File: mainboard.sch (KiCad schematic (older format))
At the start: 41 parts

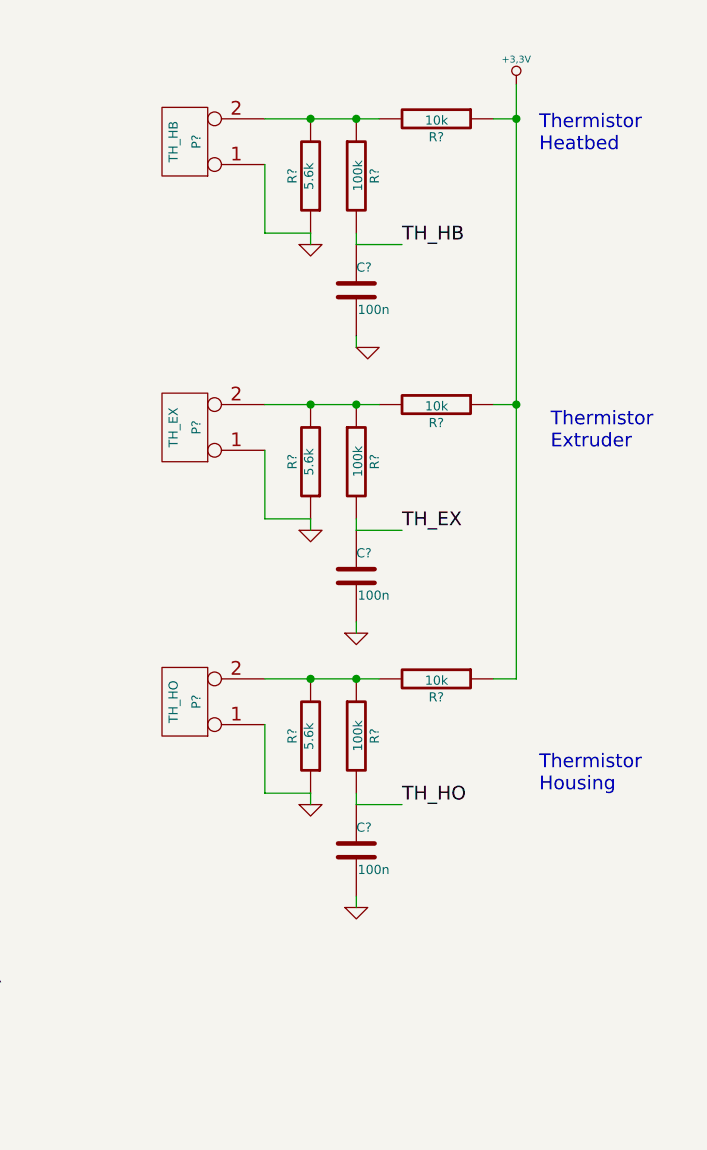
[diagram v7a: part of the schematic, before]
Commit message: Added Pot to trim ADC input for thermistors
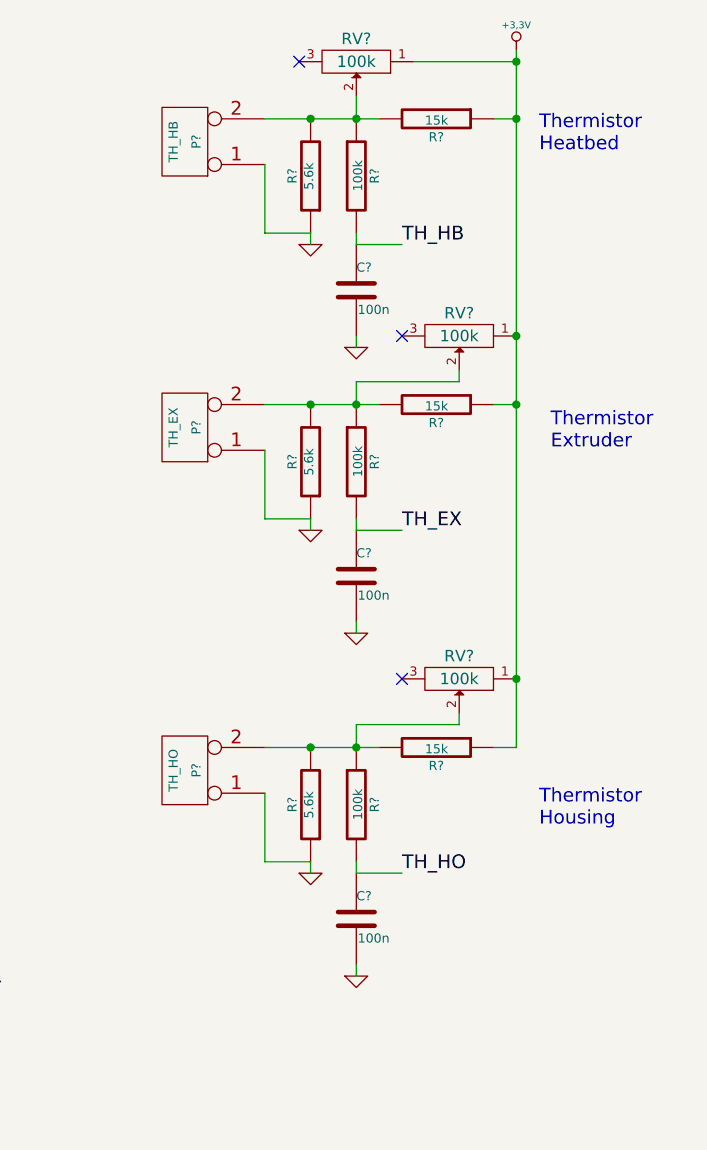
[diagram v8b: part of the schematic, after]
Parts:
- added RV? (x3): 100k, symbol POT
- R? (x3): value 10k -> 15k
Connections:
- net +3.3V: now also RV?.1, RV?.1, RV?.1
- net GND: now also C?.2
- net at P?.2 (PM), R?.1, R?.2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: now also RV?.2 (x3)
- no-connect marks 1 -> 4
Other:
- moved on the sheet: C?, P?, R?
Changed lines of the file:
@@
 P 10200 950
 F 0 "R?" V 10280 950 40  0000 C CNN
-F 1 "10k" V 10207 951 40  0000 C CNN
+F 1 "15k" V 10207 951 40  0000 C CNN
 F 2 "" V 10130 950 30  0000 C CNN
 F 3 "" H 10200 950 30  0000 C CNN
@@
 L +3,3V #PWR?
 U 1 1 53332328
-P 10550 800
-F 0 "#PWR?" H 10550 760 30  0001 C CNN
-F 1 "+3,3V" H 10550 910 30  0000 C CNN
-F 2 "" H 10550 800 60  0000 C CNN
-F 3 "" H 10550 800 60  0000 C CNN
-	1    10550 800
+P 10550 650
+F 0 "#PWR?" H 10550 610 30  0001 C CNN
+F 1 "+3,3V" H 10550 760 30  0000 C CNN
+F 2 "" H 10550 650 60  0000 C CNN
+F 3 "" H 10550 650 60  0000 C CNN
+	1    10550 650
 	1    0    0    -1
 $EndComp
@@
 Text Notes 10700 2400 0    60   ~ 0
 Thermistor\nExtruder
-Text Notes 10650 3900 0    60   ~ 0
+Text Notes 10650 4050 0    60   ~ 0
 Thermistor\nHousing
 Text Label 10050 1500 0    60   ~ 0
@@
 Text Label 10050 2750 0    60   ~ 0
 TH_EX
-Text Label 10050 3950 0    60   ~ 0
+Text Label 10050 4250 0    60   ~ 0
 TH_HO
 Text Label 4250 4100 0    60   ~ 0
@@
 L GND #PWR?
 U 1 1 5337302A
-P 9900 1950
-F 0 "#PWR?" H 9900 1950 30  0001 C CNN
-F 1 "GND" H 9900 1880 30  0001 C CNN
-F 2 "" H 9900 1950 60  0000 C CNN
-F 3 "" H 9900 1950 60  0000 C CNN
-	1    9900 1950
+P 9850 1950
+F 0 "#PWR?" H 9850 1950 30  0001 C CNN
+F 1 "GND" H 9850 1880 30  0001 C CNN
+F 2 "" H 9850 1950 60  0000 C CNN
+F 3 "" H 9850 1950 60  0000 C CNN
+	1    9850 1950
 	1    0    0    -1
 $EndComp
@@
 P 10200 2200
 F 0 "R?" V 10280 2200 40  0000 C CNN
-F 1 "10k" V 10207 2201 40  0000 C CNN
+F 1 "15k" V 10207 2201 40  0000 C CNN
 F 2 "" V 10130 2200 30  0000 C CNN
 F 3 "" H 10200 2200 30  0000 C CNN
@@
 L CONN_2 P?
 U 1 1 53373631
-P 9100 3500
-F 0 "P?" V 9050 3500 40  0000 C CNN
-F 1 "TH_HO" V 9150 3500 40  0000 C CNN
-F 2 "" H 9100 3500 60  0000 C CNN
-F 3 "" H 9100 3500 60  0000 C CNN
-	1    9100 3500
+P 9100 3800
+F 0 "P?" V 9050 3800 40  0000 C CNN
+F 1 "TH_HO" V 9150 3800 40  0000 C CNN
+F 2 "" H 9100 3800 60  0000 C CNN
+F 3 "" H 9100 3800 60  0000 C CNN
+	1    9100 3800
 	-1   0    0    1
 $EndComp
@@
 L R R?
 U 1 1 53373637
-P 10200 3400
-F 0 "R?" V 10280 3400 40  0000 C CNN
-F 1 "10k" V 10207 3401 40  0000 C CNN
-F 2 "" V 10130 3400 30  0000 C CNN
-F 3 "" H 10200 3400 30  0000 C CNN
-	1    10200 3400
+P 10200 3700
+F 0 "R?" V 10280 3700 40  0000 C CNN
+F 1 "15k" V 10207 3701 40  0000 C CNN
+F 2 "" V 10130 3700 30  0000 C CNN
+F 3 "" H 10200 3700 30  0000 C CNN
+	1    10200 3700
 	0    1    1    0
 $EndComp
@@
 L GND #PWR?
 U 1 1 5337363D
-P 9650 3950
-F 0 "#PWR?" H 9650 3950 30  0001 C CNN
-F 1 "GND" H 9650 3880 30  0001 C CNN
-F 2 "" H 9650 3950 60  0000 C CNN
-F 3 "" H 9650 3950 60  0000 C CNN
-	1    9650 3950
+P 9650 4250
+F 0 "#PWR?" H 9650 4250 30  0001 C CNN
+F 1 "GND" H 9650 4180 30  0001 C CNN
+F 2 "" H 9650 4250 60  0000 C CNN
+F 3 "" H 9650 4250 60  0000 C CNN
+	1    9650 4250
 	1    0    0    -1
 $EndComp
@@
 L C C?
 U 1 1 53373644
-P 9850 4150
-F 0 "C?" H 9850 4250 40  0000 L CNN
-F 1 "100n" H 9856 4065 40  0000 L CNN
-F 2 "" H 9888 4000 30  0000 C CNN
-F 3 "" H 9850 4150 60  0000 C CNN
-	1    9850 4150
+P 9850 4450
+F 0 "C?" H 9850 4550 40  0000 L CNN
+F 1 "100n" H 9856 4365 40  0000 L CNN
+F 2 "" H 9888 4300 30  0000 C CNN
+F 3 "" H 9850 4450 60  0000 C CNN
+	1    9850 4450
 	1    0    0    -1
 $EndComp
@@
 L R R?
 U 1 1 5337364A
-P 9850 3650
-F 0 "R?" V 9930 3650 40  0000 C CNN
-F 1 "100k" V 9857 3651 40  0000 C CNN
-F 2 "" V 9780 3650 30  0000 C CNN
-F 3 "" H 9850 3650 30  0000 C CNN
-	1    9850 3650
+P 9850 3950
+F 0 "R?" V 9930 3950 40  0000 C CNN
+F 1 "100k" V 9857 3951 40  0000 C CNN
+F 2 "" V 9780 3950 30  0000 C CNN
+F 3 "" H 9850 3950 30  0000 C CNN
+	1    9850 3950
 	1    0    0    -1
 $EndComp
@@
 L R R?
 U 1 1 53373650
-P 9650 3650
-F 0 "R?" V 9730 3650 40  0000 C CNN
-F 1 "5.6k" V 9657 3651 40  0000 C CNN
-F 2 "" V 9580 3650 30  0000 C CNN
-F 3 "" H 9650 3650 30  0000 C CNN
-	1    9650 3650
+P 9650 3950
+F 0 "R?" V 9730 3950 40  0000 C CNN
+F 1 "5.6k" V 9657 3951 40  0000 C CNN
+F 2 "" V 9580 3950 30  0000 C CNN
+F 3 "" H 9650 3950 30  0000 C CNN
+	1    9650 3950
 	-1   0    0    1
 $EndComp
@@
 L GND #PWR?
 U 1 1 5337365B
-P 9850 4400
-F 0 "#PWR?" H 9850 4400 30  0001 C CNN
-F 1 "GND" H 9850 4330 30  0001 C CNN
-F 2 "" H 9850 4400 60  0000 C CNN
-F 3 "" H 9850 4400 60  0000 C CNN
-	1    9850 4400
+P 9850 4700
+F 0 "#PWR?" H 9850 4700 30  0001 C CNN
+F 1 "GND" H 9850 4630 30  0001 C CNN
+F 2 "" H 9850 4700 60  0000 C CNN
+F 3 "" H 9850 4700 60  0000 C CNN
+	1    9850 4700
 	1    0    0    -1
 $EndComp
@@
 	9450 2700 9650 2700
 Wire Wire Line
-	9650 3950 9650 3900
-Connection ~ 9650 3400
-Connection ~ 9850 3400
-Wire Wire Line
-	9850 3950 9850 3900
-Wire Wire Line
-	10050 3950 9850 3950
-Wire Wire Line
-	9850 4400 9850 4350
-Wire Wire Line
-	9450 3400 9950 3400
-Wire Wire Line
-	9450 3600 9450 3900
-Wire Wire Line
-	9450 3900 9650 3900
+	9650 4250 9650 4200
+Connection ~ 9650 3700
+Connection ~ 9850 3700
+Wire Wire Line
+	9850 4250 9850 4200
+Wire Wire Line
+	10050 4250 9850 4250
+Wire Wire Line
+	9850 4700 9850 4650
+Wire Wire Line
+	9450 3700 9950 3700
+Wire Wire Line
+	9450 3900 9450 4200
+Wire Wire Line
+	9450 4200 9650 4200
 Connection ~ 10550 950
 Wire Wire Line
-	10450 2200 10550 2200
-Wire Wire Line
-	10550 3400 10450 3400
-Wire Wire Line
-	10550 800  10550 3400
+	10550 2200 10450 2200
+Wire Wire Line
+	10550 3700 10450 3700
+$Comp
+L POT RV?
+U 1 1 5337E0EF
+P 10300 3400
+F 0 "RV?" H 10300 3300 50  0000 C CNN
+F 1 "100k" H 10300 3400 50  0000 C CNN
+F 2 "" H 10300 3400 60  0000 C CNN
+F 3 "" H 10300 3400 60  0000 C CNN
+	1    10300 3400
+	-1   0    0    1
+$EndComp
+Connection ~ 10550 3400
+NoConn ~ 10050 3400
+Wire Wire Line
+	10550 650  10550 3700
+Wire Wire Line
+	10300 3550 10300 3600
+Wire Wire Line
+	10300 3600 9850 3600
+Wire Wire Line
+	9850 3600 9850 3700
+$Comp
+L POT RV?
+U 1 1 5337E930
+P 10300 1900
+F 0 "RV?" H 10300 1800 50  0000 C CNN
+F 1 "100k" H 10300 1900 50  0000 C CNN
+F 2 "" H 10300 1900 60  0000 C CNN
+F 3 "" H 10300 1900 60  0000 C CNN
+	1    10300 1900
+	-1   0    0    1
+$EndComp
+NoConn ~ 10050 1900
+Wire Wire Line
+	10300 2050 10300 2100
+Wire Wire Line
+	10300 2100 9850 2100
+Wire Wire Line
+	9850 2100 9850 2200
+Connection ~ 10550 1900
+$Comp
+L POT RV?
+U 1 1 5337EA04
+P 9850 700
+F 0 "RV?" H 9850 600 50  0000 C CNN
+F 1 "100k" H 9850 700 50  0000 C CNN
+F 2 "" H 9850 700 60  0000 C CNN
+F 3 "" H 9850 700 60  0000 C CNN
+	1    9850 700
+	-1   0    0    1
+$EndComp
+NoConn ~ 9600 700
+Wire Wire Line
+	10100 700  10550 700
+Wire Wire Line
+	9850 850  9850 950
+Connection ~ 10550 700
 $EndSCHEMATC
